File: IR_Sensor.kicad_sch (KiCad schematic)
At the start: 30 parts, among them J8 Conn_01x03_Female, Q1 AO3401, Q3 NJL7302L-F3, Q31 Q_NPN_BEC, U12 AE-BME280, U17 OSRB38C9AA

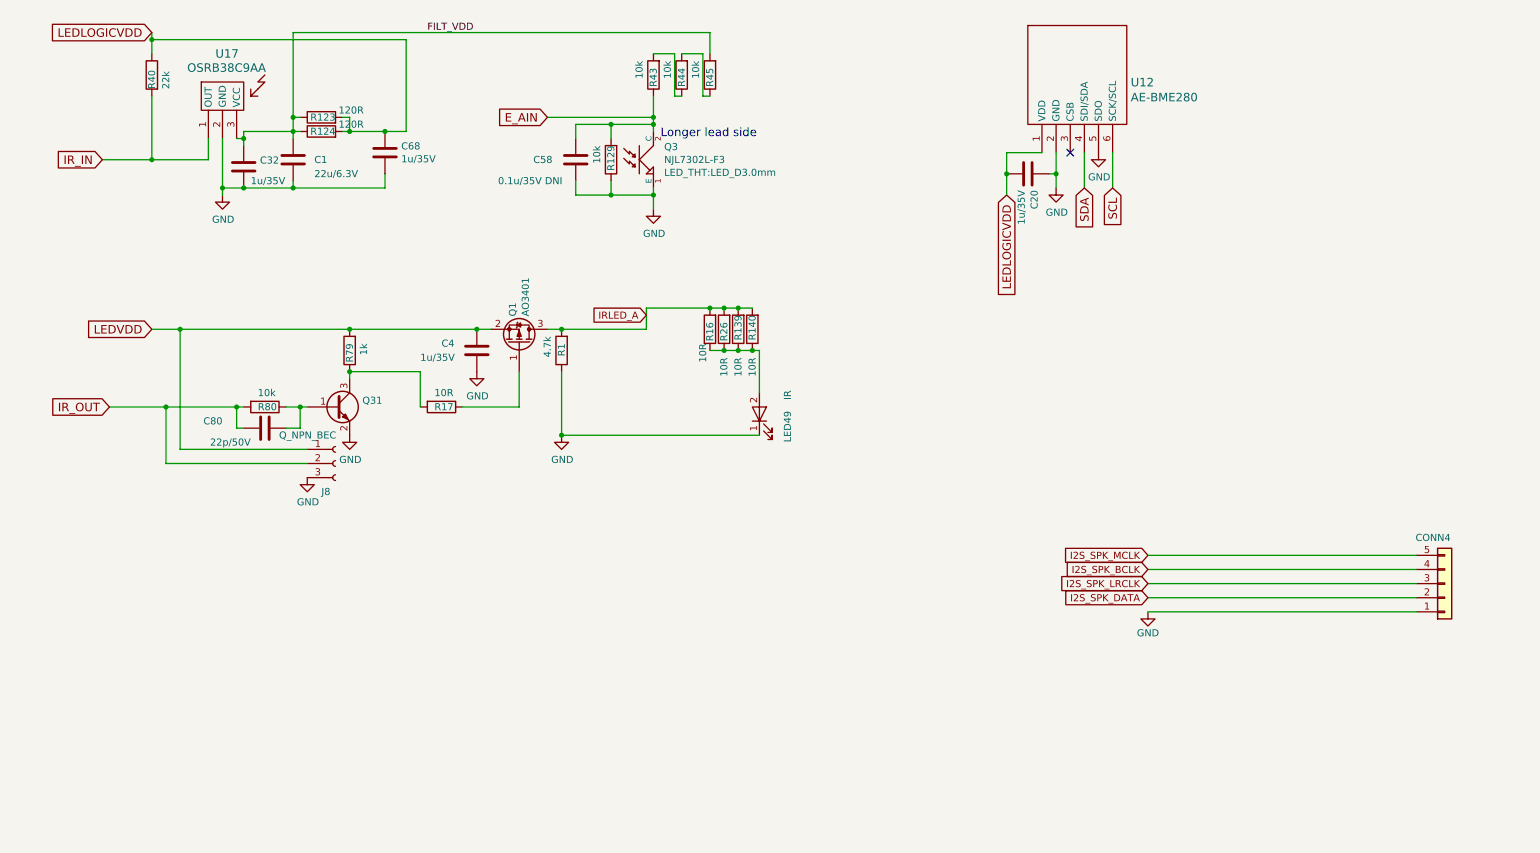
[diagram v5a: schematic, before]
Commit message: WROOM32 coupling capacitor order fixed; Added FB on long line to board left-most sensors
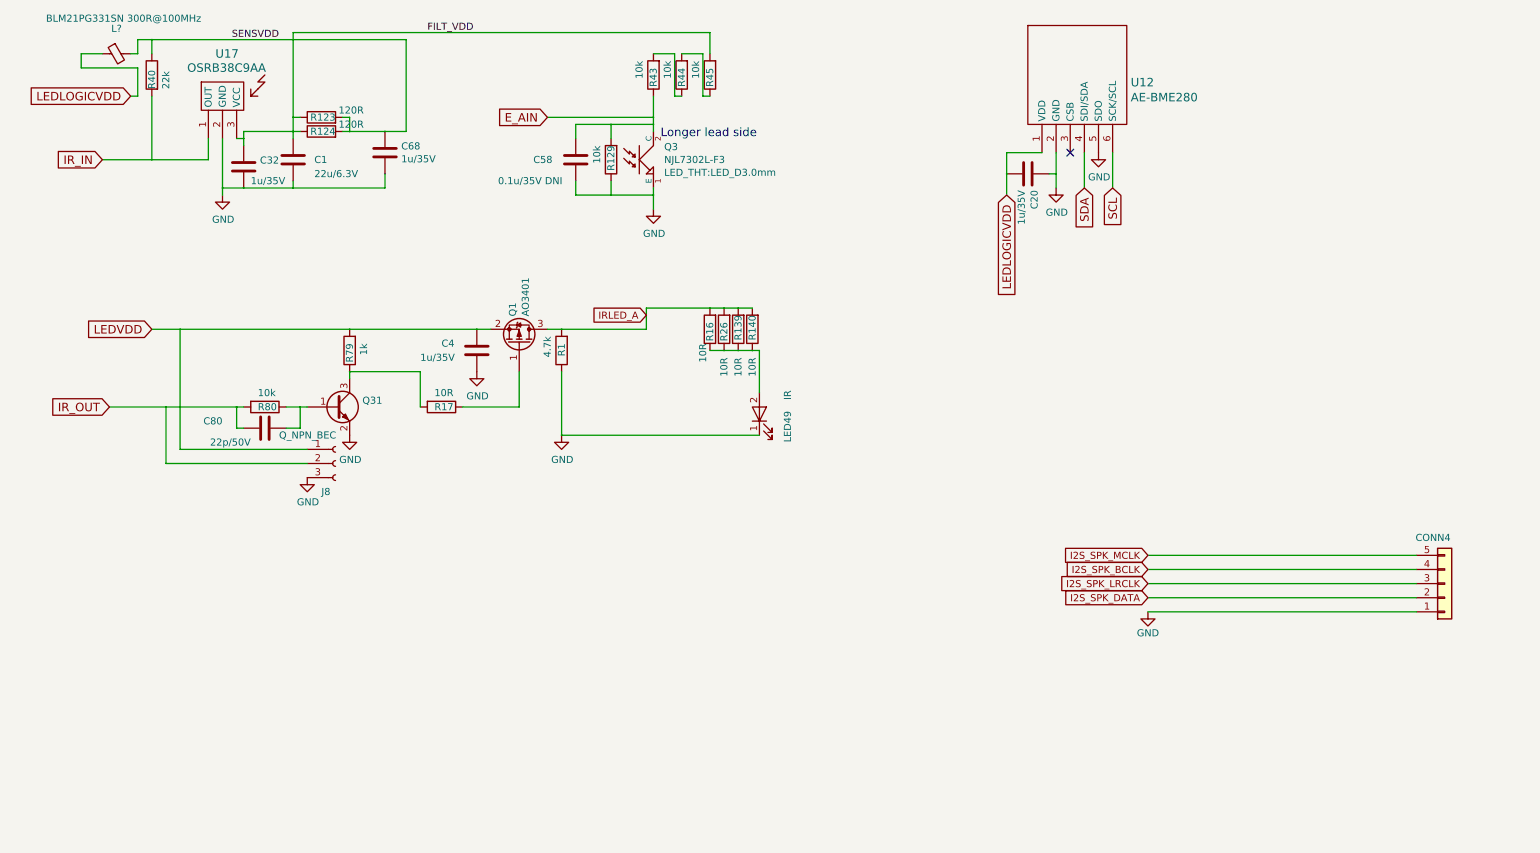
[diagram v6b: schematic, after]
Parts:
- added L?: BLM21PG331SN 300R@100MHz, Capacitor_SMD:C_0805_2012Metric_Pad1.15x1.40mm_HandSolder, symbol dotmatrix_64x48-rescue:Ferrite_Bead_Small-device
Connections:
- net LEDLOGICVDD: now also L?.1; no longer C68.1, R123.2, R124.2, R40.1
- new net SENSVDD: C68.1, L?.2, R123.2, R124.2, R40.1
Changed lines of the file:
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@@
-(kicad_sch (version 20200618) (host eeschema "5.99.0-unknown-7340c97~89~ubuntu18.04.1")
-  (page 1 10)
+(kicad_sch (version 20200714) (host eeschema "5.99.0-unknown-e5f2015a9~89~ubuntu18.04.1")
+  (page 2 10)
   (paper "A4")
-  (junction (at 34.29 17.78) (diameter 0) (color 0 0 0 0))
-  (junction (at 34.29 39.37) (diameter 0) (color 0 0 0 0))
-  (junction (at 36.83 83.82) (diameter 0) (color 0 0 0 0))
-  (junction (at 39.37 69.85) (diameter 0) (color 0 0 0 0))
-  (junction (at 46.99 44.45) (diameter 0) (color 0 0 0 0))
-  (junction (at 49.53 83.82) (diameter 0) (color 0 0 0 0))
-  (junction (at 50.8 35.56) (diameter 0) (color 0 0 0 0))
-  (junction (at 50.8 44.45) (diameter 0) (color 0 0 0 0))
-  (junction (at 59.69 31.75) (diameter 0) (color 0 0 0 0))
-  (junction (at 59.69 34.29) (diameter 0) (color 0 0 0 0))
-  (junction (at 59.69 44.45) (diameter 0) (color 0 0 0 0))
-  (junction (at 60.96 83.82) (diameter 0) (color 0 0 0 0))
-  (junction (at 69.85 34.29) (diameter 0) (color 0 0 0 0))
-  (junction (at 69.85 69.85) (diameter 0) (color 0 0 0 0))
-  (junction (at 69.85 77.47) (diameter 0) (color 0 0 0 0))
-  (junction (at 76.2 34.29) (diameter 0) (color 0 0 0 0))
-  (junction (at 92.71 69.85) (diameter 0) (color 0 0 0 0))
-  (junction (at 107.95 69.85) (diameter 0) (color 0 0 0 0))
-  (junction (at 107.95 88.9) (diameter 0) (color 0 0 0 0))
-  (junction (at 116.84 33.02) (diameter 0) (color 0 0 0 0))
-  (junction (at 116.84 45.72) (diameter 0) (color 0 0 0 0))
-  (junction (at 124.46 31.75) (diameter 0) (color 0 0 0 0))
-  (junction (at 124.46 33.02) (diameter 0) (color 0 0 0 0))
-  (junction (at 124.46 45.72) (diameter 0) (color 0 0 0 0))
-  (junction (at 134.62 66.04) (diameter 0) (color 0 0 0 0))
-  (junction (at 137.16 66.04) (diameter 0) (color 0 0 0 0))
-  (junction (at 137.16 73.66) (diameter 0) (color 0 0 0 0))
-  (junction (at 139.7 66.04) (diameter 0) (color 0 0 0 0))
-  (junction (at 139.7 73.66) (diameter 0) (color 0 0 0 0))
-  (junction (at 142.24 73.66) (diameter 0) (color 0 0 0 0))
-  (junction (at 187.96 41.91) (diameter 0) (color 0 0 0 0))
-  (junction (at 196.85 41.91) (diameter 0) (color 0 0 0 0))
+  (junction (at 34.29 17.78) (diameter 0.3048) (color 0 0 0 0))
+  (junction (at 34.29 39.37) (diameter 0.3048) (color 0 0 0 0))
+  (junction (at 36.83 83.82) (diameter 0.3048) (color 0 0 0 0))
+  (junction (at 39.37 69.85) (diameter 0.3048) (color 0 0 0 0))
+  (junction (at 46.99 44.45) (diameter 0.3048) (color 0 0 0 0))
+  (junction (at 49.53 83.82) (diameter 0.3048) (color 0 0 0 0))
+  (junction (at 50.8 35.56) (diameter 0.3048) (color 0 0 0 0))
+  (junction (at 50.8 44.45) (diameter 0.3048) (color 0 0 0 0))
+  (junction (at 59.69 31.75) (diameter 0.3048) (color 0 0 0 0))
+  (junction (at 59.69 34.29) (diameter 0.3048) (color 0 0 0 0))
+  (junction (at 59.69 44.45) (diameter 0.3048) (color 0 0 0 0))
+  (junction (at 60.96 83.82) (diameter 0.3048) (color 0 0 0 0))
+  (junction (at 69.85 34.29) (diameter 0.3048) (color 0 0 0 0))
+  (junction (at 69.85 69.85) (diameter 0.3048) (color 0 0 0 0))
+  (junction (at 69.85 77.47) (diameter 0.3048) (color 0 0 0 0))
+  (junction (at 76.2 34.29) (diameter 0.3048) (color 0 0 0 0))
+  (junction (at 92.71 69.85) (diameter 0.3048) (color 0 0 0 0))
+  (junction (at 107.95 69.85) (diameter 0.3048) (color 0 0 0 0))
+  (junction (at 107.95 88.9) (diameter 0.3048) (color 0 0 0 0))
+  (junction (at 116.84 33.02) (diameter 0.3048) (color 0 0 0 0))
+  (junction (at 116.84 45.72) (diameter 0.3048) (color 0 0 0 0))
+  (junction (at 124.46 31.75) (diameter 0.3048) (color 0 0 0 0))
+  (junction (at 124.46 33.02) (diameter 0.3048) (color 0 0 0 0))
+  (junction (at 124.46 45.72) (diameter 0.3048) (color 0 0 0 0))
+  (junction (at 134.62 66.04) (diameter 0.3048) (color 0 0 0 0))
+  (junction (at 137.16 66.04) (diameter 0.3048) (color 0 0 0 0))
+  (junction (at 137.16 73.66) (diameter 0.3048) (color 0 0 0 0))
+  (junction (at 139.7 66.04) (diameter 0.3048) (color 0 0 0 0))
+  (junction (at 139.7 73.66) (diameter 0.3048) (color 0 0 0 0))
+  (junction (at 142.24 73.66) (diameter 0.3048) (color 0 0 0 0))
+  (junction (at 187.96 41.91) (diameter 0.3048) (color 0 0 0 0))
+  (junction (at 196.85 41.91) (diameter 0.3048) (color 0 0 0 0))
   (no_connect (at 199.39 38.1))
+  (wire (pts (xy 21.59 20.32) (xy 25.4 20.32))
+    (stroke (width 0) (type solid) (color 0 0 0 0))
+  )
+  (wire (pts (xy 21.59 22.86) (xy 21.59 20.32))
+    (stroke (width 0) (type solid) (color 0 0 0 0))
+  )
   (wire (pts (xy 25.4 39.37) (xy 34.29 39.37))
     (stroke (width 0) (type solid) (color 0 0 0 0))
@@
     (stroke (width 0) (type solid) (color 0 0 0 0))
   )
-  (wire (pts (xy 34.29 17.78) (xy 34.29 16.51))
-    (stroke (width 0) (type solid) (color 0 0 0 0))
-  )
-  (wire (pts (xy 34.29 20.32) (xy 34.29 17.78))
+  (wire (pts (xy 30.48 20.32) (xy 31.75 20.32))
+    (stroke (width 0) (type solid) (color 0 0 0 0))
+  )
+  (wire (pts (xy 30.48 27.94) (xy 31.75 27.94))
+    (stroke (width 0) (type solid) (color 0 0 0 0))
+  )
+  (wire (pts (xy 31.75 17.78) (xy 34.29 17.78))
+    (stroke (width 0) (type solid) (color 0 0 0 0))
+  )
+  (wire (pts (xy 31.75 20.32) (xy 31.75 17.78))
+    (stroke (width 0) (type solid) (color 0 0 0 0))
+  )
+  (wire (pts (xy 31.75 22.86) (xy 21.59 22.86))
+    (stroke (width 0) (type solid) (color 0 0 0 0))
+  )
+  (wire (pts (xy 31.75 27.94) (xy 31.75 22.86))
+    (stroke (width 0) (type solid) (color 0 0 0 0))
+  )
+  (wire (pts (xy 34.29 17.78) (xy 34.29 20.32))
     (stroke (width 0) (type solid) (color 0 0 0 0))
   )
@@
     (effects (font (size 1.524 1.524)) (justify left bottom))
   )
+  (label "SENSVDD" (at 57.15 17.78 180)
+    (effects (font (size 1.27 1.27)) (justify right bottom))
+  )
   (label "FILT_VDD" (at 83.82 16.51 0)
     (effects (font (size 1.27 1.27)) (justify left bottom))
@@
     (effects (font (size 1.524 1.524)) (justify right))
   )
-  (global_label "LEDLOGICVDD" (shape input) (at 34.29 16.51 180)
+  (global_label "LEDLOGICVDD" (shape input) (at 30.48 27.94 180)
     (effects (font (size 1.524 1.524)) (justify right))
   )
@@
     (property "Datasheet" "" (id 3) (at 142.24 69.85 0))
   )
+  (symbol (lib_id "dotmatrix_64x48-rescue:Ferrite_Bead_Small-device") (at 27.94 20.32 90) (mirror x) (unit 1)
+    (in_bom yes) (on_board yes)
+    (property "Reference" "L?" (id 0) (at 27.94 15.7988 90))
+    (property "Value" "BLM21PG331SN 300R@100MHz" (id 1) (at 29.21 13.97 90))
+    (property "Footprint" "Capacitor_SMD:C_0805_2012Metric_Pad1.15x1.40mm_HandSolder" (id 2) (at 27.94 20.32 0)
+      (effects (font (size 1.27 1.27)) hide)
+    )
+    (property "Datasheet" "" (id 3) (at 27.94 20.32 0))
+  )
   (symbol (lib_id "dotmatrix_64x48-rescue:LED-device") (at 143.51 85.09 90) (unit 1)

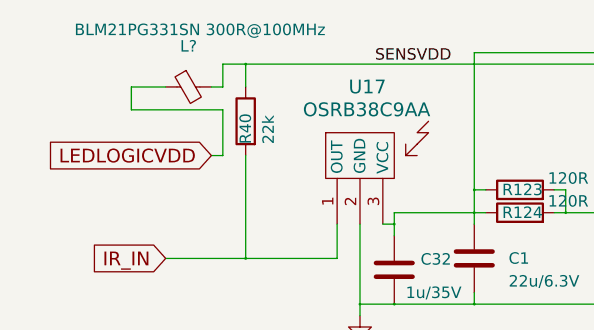
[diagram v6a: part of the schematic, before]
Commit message: Changed from USB micro-B to Type C. DRC should be clear.
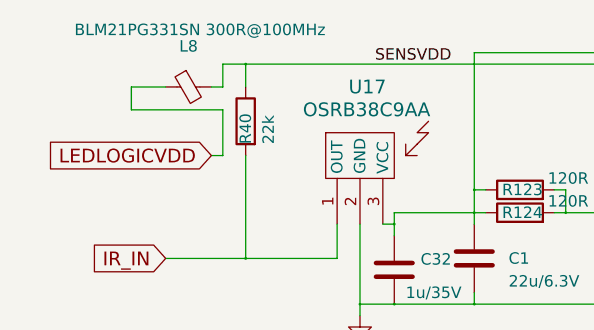
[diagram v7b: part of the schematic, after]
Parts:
- gave numbers to parts that had none: 1
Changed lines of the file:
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@@
-(kicad_sch (version 20200714) (host eeschema "5.99.0-unknown-e5f2015a9~89~ubuntu18.04.1")
+(kicad_sch (version 20200714) (host eeschema "5.99.0-unknown-3ddee6503~89~ubuntu18.04.1")
   (page 2 10)
   (paper "A4")
@@
   (symbol (lib_id "dotmatrix_64x48-rescue:Ferrite_Bead_Small-device") (at 27.94 20.32 90) (mirror x) (unit 1)
     (in_bom yes) (on_board yes)
-    (property "Reference" "L?" (id 0) (at 27.94 15.7988 90))
+    (property "Reference" "L8" (id 0) (at 27.94 15.7988 90))
     (property "Value" "BLM21PG331SN 300R@100MHz" (id 1) (at 29.21 13.97 90))
     (property "Footprint" "Capacitor_SMD:C_0805_2012Metric_Pad1.15x1.40mm_HandSolder" (id 2) (at 27.94 20.32 0)
